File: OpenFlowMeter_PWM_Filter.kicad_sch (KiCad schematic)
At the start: 12 parts, among them U3 LT1492

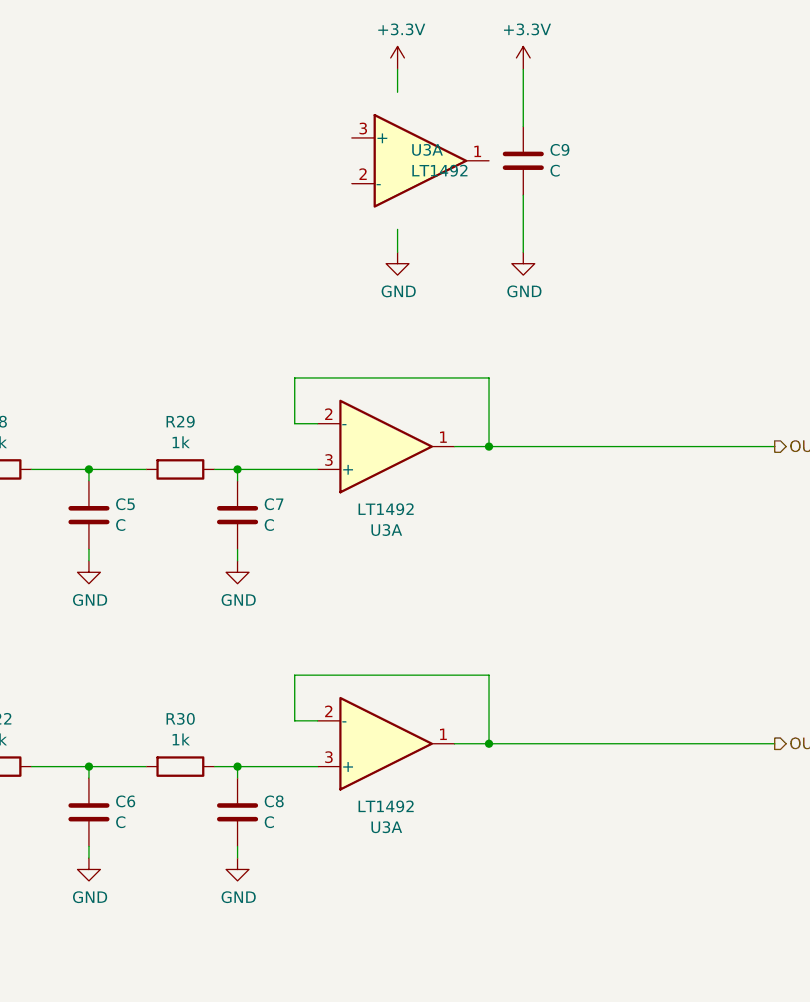
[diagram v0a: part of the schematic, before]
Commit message: intermediate commit
updated schematics and started with controller section

layout proceeded with PWM filter
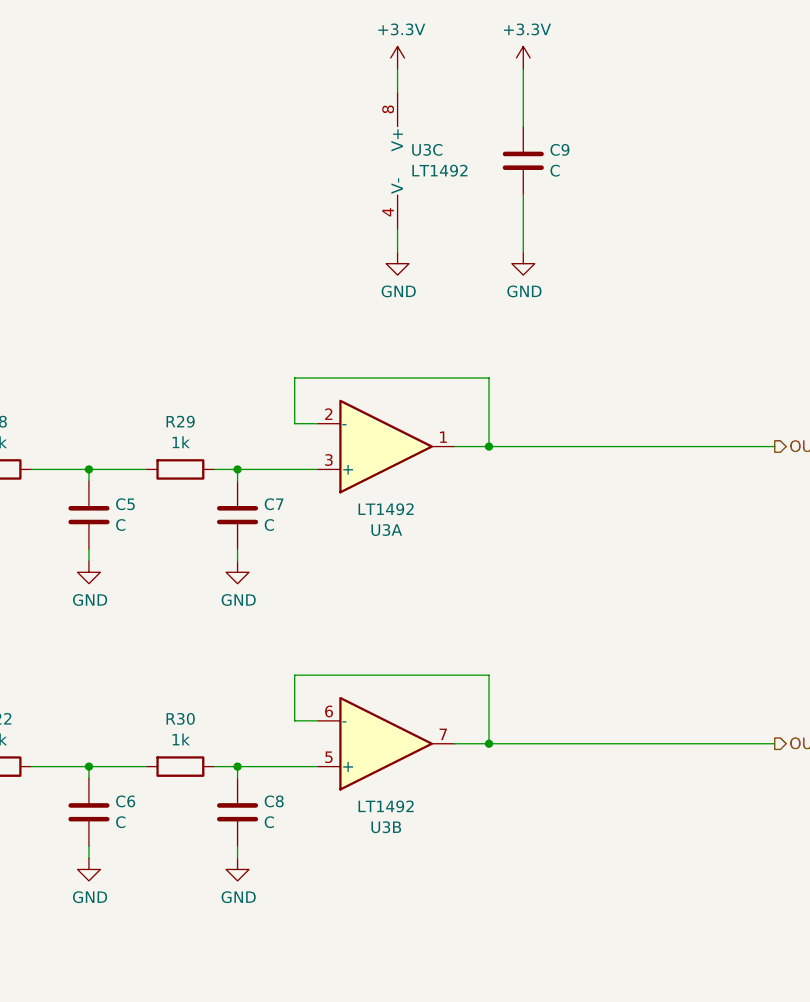
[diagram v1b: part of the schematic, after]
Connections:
- net +3V3: now also U3.8 (V+)
- net GND: now also U3.4 (V-)
- net OUT2: now also U3.6 (-), U3.7; no longer U3.1, U3.2 (-)
- net at C8.1, R30.1: now also U3.5 (+); no longer U3.3 (+)
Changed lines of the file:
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@@
     (effects (font (size 1.27 1.27)) (justify right))
   )
-  (symbol (lib_id "Amplifier_Operational:LT1492") (at 147.32 91.44 0) (mirror x)
+  (symbol (lib_id "Amplifier_Operational:LT1492") (at 147.32 91.44 0) (mirror x) (unit 1)
     (in_bom yes) (on_board yes)
     (property "Reference" "U3" (id 0) (at 147.32 100.7618 0))
@@
     (pin "3")
   )
-  (symbol (lib_id "Amplifier_Operational:LT1492") (at 151.13 59.69 0)
+  (symbol (lib_id "Amplifier_Operational:LT1492") (at 151.13 59.69 0) (unit 3)
     (in_bom yes) (on_board yes)
     (property "Reference" "U3" (id 0) (at 150.0632 58.5216 0)
@@
     (pin "8")
   )
-  (symbol (lib_id "power:GND") (at 148.59 69.85 0)
+  (symbol (lib_id "power:GND") (at 148.59 69.85 0) (unit 1)
     (in_bom yes) (on_board yes)
     (property "Reference" "#PWR017" (id 0) (at 148.59 76.2 0)
@@
     (pin "1")
   )
-  (symbol (lib_id "Device:C") (at 162.56 59.69 0)
+  (symbol (lib_id "Device:C") (at 162.56 59.69 0) (unit 1)
     (in_bom yes) (on_board yes)
     (property "Reference" "C9" (id 0) (at 165.481 58.5216 0)
@@
     (pin "2")
   )
-  (symbol (lib_id "power:GND") (at 162.56 69.85 0)
+  (symbol (lib_id "power:GND") (at 162.56 69.85 0) (unit 1)
     (in_bom yes) (on_board yes)
     (property "Reference" "#PWR018" (id 0) (at 162.56 76.2 0)
@@
     (pin "1")
   )
-  (symbol (lib_id "Amplifier_Operational:LT1492") (at 147.32 124.46 0) (mirror x)
+  (symbol (lib_id "Amplifier_Operational:LT1492") (at 147.32 124.46 0) (mirror x) (unit 2)
     (in_bom yes) (on_board yes)
     (property "Reference" "U3" (id 0) (at 147.32 133.7818 0))
@@
     (pin "7")
   )
-  (symbol (lib_id "Device:R") (at 104.14 93.98 270)
+  (symbol (lib_id "Device:R") (at 104.14 93.98 270) (unit 1)
     (in_bom yes) (on_board yes)
     (property "Reference" "R8" (id 0) (at 104.14 88.7222 90))
@@
     (pin "2")
   )
-  (symbol (lib_id "Device:R") (at 124.46 93.98 270)
+  (symbol (lib_id "Device:R") (at 124.46 93.98 270) (unit 1)
     (in_bom yes) (on_board yes)
     (property "Reference" "R29" (id 0) (at 124.46 88.7222 90))
@@
     (pin "2")
   )
-  (symbol (lib_id "Device:C") (at 114.3 99.06 0)
+  (symbol (lib_id "Device:C") (at 114.3 99.06 0) (unit 1)
     (in_bom yes) (on_board yes)
     (property "Reference" "C5" (id 0) (at 117.221 97.8916 0)
@@
     (pin "2")
   )
-  (symbol (lib_id "Device:C") (at 130.81 99.06 0)
+  (symbol (lib_id "Device:C") (at 130.81 99.06 0) (unit 1)
     (in_bom yes) (on_board yes)
     (property "Reference" "C7" (id 0) (at 133.731 97.8916 0)
@@
     (pin "2")
   )
-  (symbol (lib_id "power:GND") (at 130.81 104.14 0)
+  (symbol (lib_id "power:GND") (at 130.81 104.14 0) (unit 1)
     (in_bom yes) (on_board yes)
     (property "Reference" "#PWR09" (id 0) (at 130.81 110.49 0)
@@
     (pin "1")
   )
-  (symbol (lib_id "power:GND") (at 114.3 104.14 0)
+  (symbol (lib_id "power:GND") (at 114.3 104.14 0) (unit 1)
     (in_bom yes) (on_board yes)
     (property "Reference" "#PWR01" (id 0) (at 114.3 110.49 0)
@@
     (pin "1")
   )
-  (symbol (lib_id "Device:R") (at 104.14 127 270)
+  (symbol (lib_id "Device:R") (at 104.14 127 270) (unit 1)
     (in_bom yes) (on_board yes)
     (property "Reference" "R22" (id 0) (at 104.14 121.7422 90))
@@
     (pin "2")
   )
-  (symbol (lib_id "Device:R") (at 124.46 127 270)
+  (symbol (lib_id "Device:R") (at 124.46 127 270) (unit 1)
     (in_bom yes) (on_board yes)
     (property "Reference" "R30" (id 0) (at 124.46 121.7422 90))
@@
     (pin "2")
   )
-  (symbol (lib_id "Device:C") (at 114.3 132.08 0)
+  (symbol (lib_id "Device:C") (at 114.3 132.08 0) (unit 1)
     (in_bom yes) (on_board yes)
     (property "Reference" "C6" (id 0) (at 117.221 130.9116 0)
@@
     (pin "2")
   )
-  (symbol (lib_id "Device:C") (at 130.81 132.08 0)
+  (symbol (lib_id "Device:C") (at 130.81 132.08 0) (unit 1)
     (in_bom yes) (on_board yes)
     (property "Reference" "C8" (id 0) (at 133.731 130.9116 0)
@@
     (pin "2")
   )
-  (symbol (lib_id "power:GND") (at 130.81 137.16 0)
+  (symbol (lib_id "power:GND") (at 130.81 137.16 0) (unit 1)
     (in_bom yes) (on_board yes)
     (property "Reference" "#PWR010" (id 0) (at 130.81 143.51 0)
@@
     (pin "1")
   )
-  (symbol (lib_id "power:GND") (at 114.3 137.16 0)
+  (symbol (lib_id "power:GND") (at 114.3 137.16 0) (unit 1)
     (in_bom yes) (on_board yes)
     (property "Reference" "#PWR08" (id 0) (at 114.3 143.51 0)

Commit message: unified C footprints
made all capacitor footprints the same
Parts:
- C5, C6, C7, C8, C9: footprint Capacitor_SMD:C_0603_1608Metric_Pad1.05x0.95mm_HandSolder -> Capacitor_SMD:C_0603_1608Metric_Pad1.08x0.95mm_HandSolder
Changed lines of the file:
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@@
       (effects (font (size 1.27 1.27)) (justify left))
     )
-    (property "Footprint" "Capacitor_SMD:C_0603_1608Metric_Pad1.05x0.95mm_HandSolder" (id 2) (at 163.5252 63.5 0)
+    (property "Footprint" "Capacitor_SMD:C_0603_1608Metric_Pad1.08x0.95mm_HandSolder" (id 2) (at 163.5252 63.5 0)
       (effects (font (size 1.27 1.27)) hide)
     )
@@
       (effects (font (size 1.27 1.27)) (justify left))
     )
-    (property "Footprint" "Capacitor_SMD:C_0603_1608Metric_Pad1.05x0.95mm_HandSolder" (id 2) (at 115.2652 102.87 0)
+    (property "Footprint" "Capacitor_SMD:C_0603_1608Metric_Pad1.08x0.95mm_HandSolder" (id 2) (at 115.2652 102.87 0)
       (effects (font (size 1.27 1.27)) hide)
     )
@@
       (effects (font (size 1.27 1.27)) (justify left))
     )
-    (property "Footprint" "Capacitor_SMD:C_0603_1608Metric_Pad1.05x0.95mm_HandSolder" (id 2) (at 131.7752 102.87 0)
+    (property "Footprint" "Capacitor_SMD:C_0603_1608Metric_Pad1.08x0.95mm_HandSolder" (id 2) (at 131.7752 102.87 0)
       (effects (font (size 1.27 1.27)) hide)
     )
@@
       (effects (font (size 1.27 1.27)) (justify left))
     )
-    (property "Footprint" "Capacitor_SMD:C_0603_1608Metric_Pad1.05x0.95mm_HandSolder" (id 2) (at 115.2652 135.89 0)
+    (property "Footprint" "Capacitor_SMD:C_0603_1608Metric_Pad1.08x0.95mm_HandSolder" (id 2) (at 115.2652 135.89 0)
       (effects (font (size 1.27 1.27)) hide)
     )
@@
       (effects (font (size 1.27 1.27)) (justify left))
     )
-    (property "Footprint" "Capacitor_SMD:C_0603_1608Metric_Pad1.05x0.95mm_HandSolder" (id 2) (at 131.7752 135.89 0)
+    (property "Footprint" "Capacitor_SMD:C_0603_1608Metric_Pad1.08x0.95mm_HandSolder" (id 2) (at 131.7752 135.89 0)
       (effects (font (size 1.27 1.27)) hide)
     )

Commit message: BUGFIX footprint of LT1490
Footprint of LT1490 is SOIC8 and not Micro 8 -> had to enlarge the board.
At the same step, changed all footprints from handsolder to normal solder. (saves a little space)
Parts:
- C5, C6, C7, C8, C9: footprint Capacitor_SMD:C_0603_1608Metric_Pad1.08x0.95mm_HandSolder -> Capacitor_SMD:C_0603_1608Metric
- R22, R29, R30, R8: footprint Resistor_SMD:R_0603_1608Metric_Pad0.98x0.95mm_HandSolder -> Resistor_SMD:R_0603_1608Metric
- U3: footprint Package_SO:OnSemi_Micro8 -> Package_SO:SOIC-8_3.9x4.9mm_P1.27mm
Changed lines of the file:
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@@
     (property "Reference" "U3" (id 0) (at 147.32 100.7618 0))
     (property "Value" "LT1492" (id 1) (at 147.32 98.4504 0))
-    (property "Footprint" "Package_SO:OnSemi_Micro8" (id 2) (at 147.32 91.44 0)
+    (property "Footprint" "Package_SO:SOIC-8_3.9x4.9mm_P1.27mm" (id 2) (at 147.32 91.44 0)
       (effects (font (size 1.27 1.27)) hide)
     )
@@
       (effects (font (size 1.27 1.27)) (justify left))
     )
-    (property "Footprint" "Package_SO:OnSemi_Micro8" (id 2) (at 151.13 59.69 0)
+    (property "Footprint" "Package_SO:SOIC-8_3.9x4.9mm_P1.27mm" (id 2) (at 151.13 59.69 0)
       (effects (font (size 1.27 1.27)) hide)
     )
@@
       (effects (font (size 1.27 1.27)) (justify left))
     )
-    (property "Footprint" "Capacitor_SMD:C_0603_1608Metric_Pad1.08x0.95mm_HandSolder" (id 2) (at 163.5252 63.5 0)
+    (property "Footprint" "Capacitor_SMD:C_0603_1608Metric" (id 2) (at 163.5252 63.5 0)
       (effects (font (size 1.27 1.27)) hide)
     )
@@
     (property "Reference" "U3" (id 0) (at 147.32 133.7818 0))
     (property "Value" "LT1492" (id 1) (at 147.32 131.4704 0))
-    (property "Footprint" "Package_SO:OnSemi_Micro8" (id 2) (at 147.32 124.46 0)
+    (property "Footprint" "Package_SO:SOIC-8_3.9x4.9mm_P1.27mm" (id 2) (at 147.32 124.46 0)
       (effects (font (size 1.27 1.27)) hide)
     )
@@
     (property "Reference" "R8" (id 0) (at 104.14 88.7222 90))
     (property "Value" "1k" (id 1) (at 104.14 91.0336 90))
-    (property "Footprint" "Resistor_SMD:R_0603_1608Metric_Pad0.98x0.95mm_HandSolder" (id 2) (at 104.14 92.202 90)
+    (property "Footprint" "Resistor_SMD:R_0603_1608Metric" (id 2) (at 104.14 92.202 90)
       (effects (font (size 1.27 1.27)) hide)
     )
@@
     (property "Reference" "R29" (id 0) (at 124.46 88.7222 90))
     (property "Value" "1k" (id 1) (at 124.46 91.0336 90))
-    (property "Footprint" "Resistor_SMD:R_0603_1608Metric_Pad0.98x0.95mm_HandSolder" (id 2) (at 124.46 92.202 90)
+    (property "Footprint" "Resistor_SMD:R_0603_1608Metric" (id 2) (at 124.46 92.202 90)
       (effects (font (size 1.27 1.27)) hide)
     )
@@
       (effects (font (size 1.27 1.27)) (justify left))
     )
-    (property "Footprint" "Capacitor_SMD:C_0603_1608Metric_Pad1.08x0.95mm_HandSolder" (id 2) (at 115.2652 102.87 0)
+    (property "Footprint" "Capacitor_SMD:C_0603_1608Metric" (id 2) (at 115.2652 102.87 0)
       (effects (font (size 1.27 1.27)) hide)
     )
@@
       (effects (font (size 1.27 1.27)) (justify left))
     )
-    (property "Footprint" "Capacitor_SMD:C_0603_1608Metric_Pad1.08x0.95mm_HandSolder" (id 2) (at 131.7752 102.87 0)
+    (property "Footprint" "Capacitor_SMD:C_0603_1608Metric" (id 2) (at 131.7752 102.87 0)
       (effects (font (size 1.27 1.27)) hide)
     )
@@
     (property "Reference" "R22" (id 0) (at 104.14 121.7422 90))
     (property "Value" "1k" (id 1) (at 104.14 124.0536 90))
-    (property "Footprint" "Resistor_SMD:R_0603_1608Metric_Pad0.98x0.95mm_HandSolder" (id 2) (at 104.14 125.222 90)
+    (property "Footprint" "Resistor_SMD:R_0603_1608Metric" (id 2) (at 104.14 125.222 90)
       (effects (font (size 1.27 1.27)) hide)
     )
@@
     (property "Reference" "R30" (id 0) (at 124.46 121.7422 90))
     (property "Value" "1k" (id 1) (at 124.46 124.0536 90))
-    (property "Footprint" "Resistor_SMD:R_0603_1608Metric_Pad0.98x0.95mm_HandSolder" (id 2) (at 124.46 125.222 90)
+    (property "Footprint" "Resistor_SMD:R_0603_1608Metric" (id 2) (at 124.46 125.222 90)
       (effects (font (size 1.27 1.27)) hide)
     )
@@
       (effects (font (size 1.27 1.27)) (justify left))
     )
-    (property "Footprint" "Capacitor_SMD:C_0603_1608Metric_Pad1.08x0.95mm_HandSolder" (id 2) (at 115.2652 135.89 0)
+    (property "Footprint" "Capacitor_SMD:C_0603_1608Metric" (id 2) (at 115.2652 135.89 0)
       (effects (font (size 1.27 1.27)) hide)
     )
@@
       (effects (font (size 1.27 1.27)) (justify left))
     )
-    (property "Footprint" "Capacitor_SMD:C_0603_1608Metric_Pad1.08x0.95mm_HandSolder" (id 2) (at 131.7752 135.89 0)
-      (effects (font (size 1.27 1.27)) hide)
-    )
+    (property "Footprint" "Capacitor_SMD:C_0603_1608Metric" (id 2) (at 131.7752 135.89 0)
+      (effects (font (size 1.27 1.27)) hide)
+    )

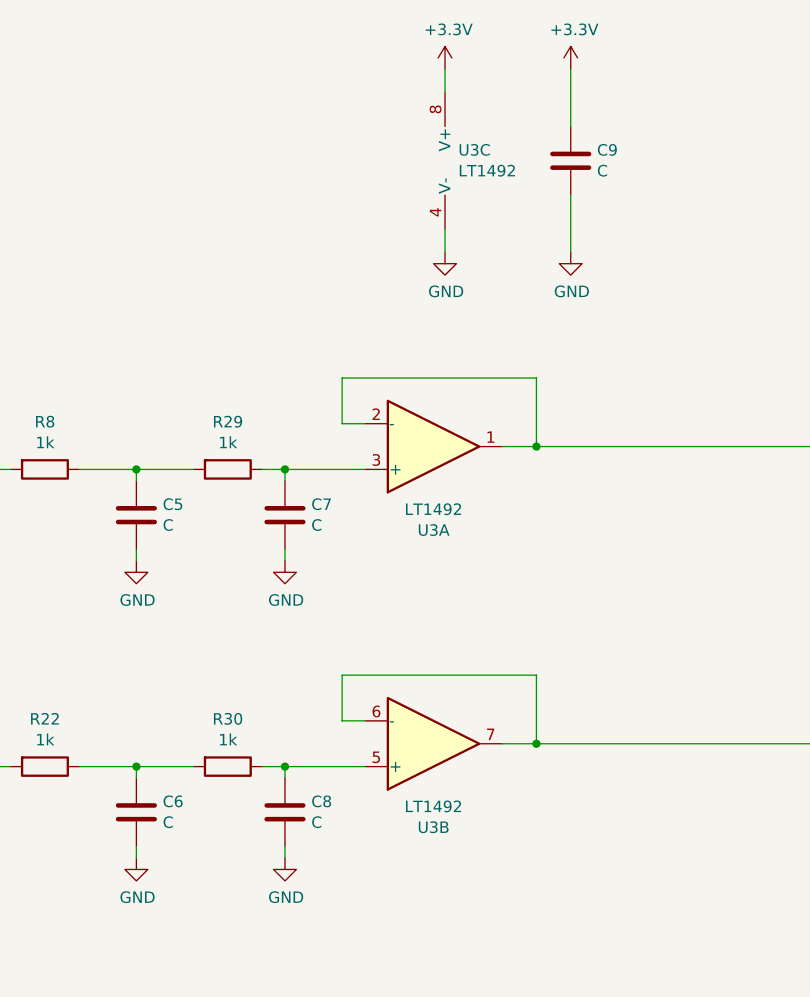
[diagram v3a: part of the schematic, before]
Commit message: added ADC protection
added Zener diodes as ADC input protection in combination with current limiting resistors.
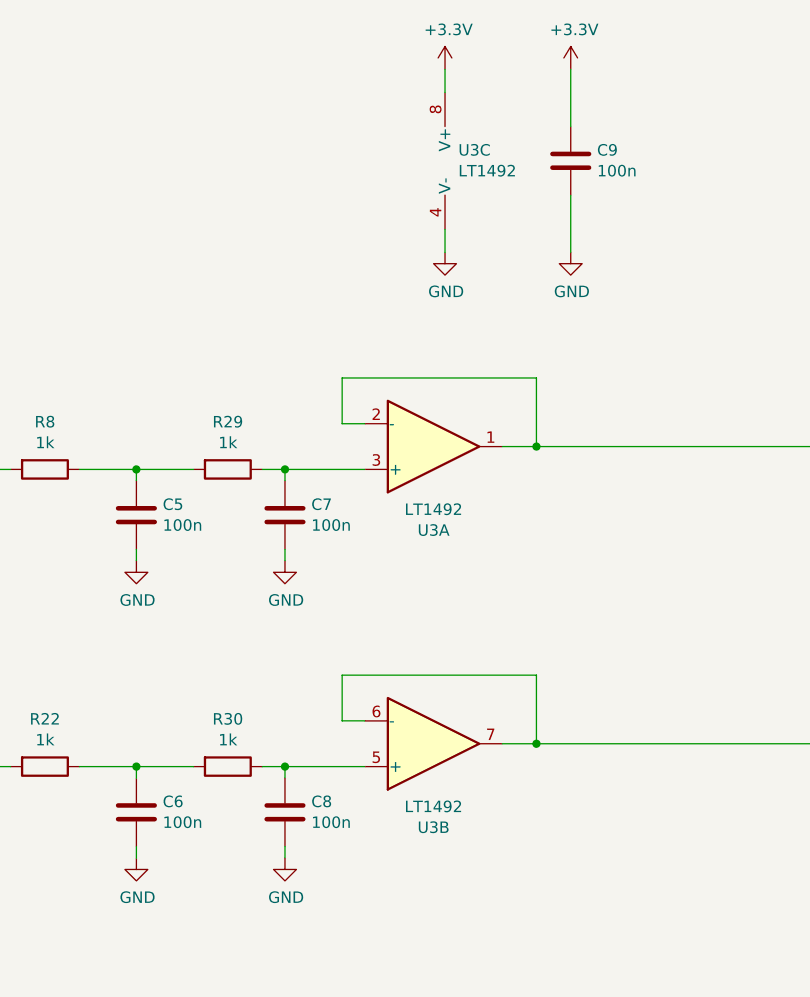
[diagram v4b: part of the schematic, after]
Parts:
- C5, C6, C7, C8, C9: value C -> 100n
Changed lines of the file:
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@@
       (effects (font (size 1.27 1.27)) (justify left))
     )
-    (property "Value" "C" (id 1) (at 165.481 60.833 0)
+    (property "Value" "100n" (id 1) (at 165.481 60.833 0)
       (effects (font (size 1.27 1.27)) (justify left))
     )
@@
       (effects (font (size 1.27 1.27)) (justify left))
     )
-    (property "Value" "C" (id 1) (at 117.221 100.203 0)
+    (property "Value" "100n" (id 1) (at 117.221 100.203 0)
       (effects (font (size 1.27 1.27)) (justify left))
     )
@@
       (effects (font (size 1.27 1.27)) (justify left))
     )
-    (property "Value" "C" (id 1) (at 133.731 100.203 0)
+    (property "Value" "100n" (id 1) (at 133.731 100.203 0)
       (effects (font (size 1.27 1.27)) (justify left))
     )
@@
       (effects (font (size 1.27 1.27)) (justify left))
     )
-    (property "Value" "C" (id 1) (at 117.221 133.223 0)
+    (property "Value" "100n" (id 1) (at 117.221 133.223 0)
       (effects (font (size 1.27 1.27)) (justify left))
     )
@@
       (effects (font (size 1.27 1.27)) (justify left))
     )
-    (property "Value" "C" (id 1) (at 133.731 133.223 0)
+    (property "Value" "100n" (id 1) (at 133.731 133.223 0)
       (effects (font (size 1.27 1.27)) (justify left))
     )
